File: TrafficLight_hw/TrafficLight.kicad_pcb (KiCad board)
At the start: 2 copper layers, 50 x 104.5 mm, 80 parts, among them Q1 BC848, Q2 MMBT2222, Q3 MMBT2222, SW1 SWITCH, SW2 DIPx6

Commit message: Proceeding with PCB
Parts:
- moved R6 76.6 mm to (139.2, 133.8), turned to 180 degrees
- moved L1 69.2 mm to (133.0, 85.0), turned to 270 degrees
- moved R14 65.5 mm to (147.6, 128.4)
- moved R13 63.2 mm to (134.8, 122.8), turned to 90 degrees
- moved R7 61.2 mm to (135.8, 133.8), turned to 180 degrees
- moved C25 59.4 mm to (142.8, 131.8), turned to 90 degrees
- moved DA1 55.3 mm to (153.2, 131.0), turned to 90 degrees
- moved R12 53.6 mm to (134.8, 119.2), turned to 90 degrees
- moved R2 51.4 mm to (149.0, 100.2), turned to 270 degrees
- moved Q2 48.2 mm to (137.8, 122.8), turned to 90 degrees
- moved Q1 46.3 mm to (137.8, 119.2), turned to 90 degrees
- moved R5 45.9 mm to (139.0, 110.2), turned to 270 degrees
- moved C24 43.5 mm to (144.6, 131.4), turned to 90 degrees
- moved C14 43.4 mm to (155.6, 131.0), turned to 270 degrees
- moved Q3 40.1 mm to (147.6, 131.4)
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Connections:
- L1 pad 2: +BATT -> +3.3V
- L2 pad 2: +BATT -> +3.3V
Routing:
- net GND: track 0.00 -> 264.3 mm, vias 0 -> 10
- net VCC: track 0.00 -> 56.9 mm, vias 0 -> 6
- net PwrMCU: track 0.00 -> 50.2 mm, vias 0 -> 4
- net +BATT: track 0.00 -> 39.5 mm
- net /IR_LED: track 0.00 -> 33.3 mm
- net /CC_MOSI: track 0.00 -> 29.1 mm, vias 0 -> 2
- net /CC_GDO2: track 0.00 -> 27.6 mm, vias 0 -> 2
- net /CC_MISO: track 0.00 -> 27.5 mm, vias 0 -> 2
- net /CC_SCK: track 0.00 -> 26.8 mm, vias 0 -> 2
- net /CC_CS: track 0.00 -> 24.5 mm
- net /CC_GDO0: track 0.00 -> 22.1 mm
- net Net-(C15-Pad1): track 0.00 -> 10.5 mm
- net Net-(C19-Pad1): track 0.00 -> 8.78 mm
- net /BAT_IN: track 0.00 -> 8.75 mm
- net /IR_LED_OUT: track 0.00 -> 7.63 mm
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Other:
- net class Default: trace_width 0.25 -> 0.2; via_dia 0.6 -> 0.7; via_drill 0.4 -> 0.3
- net class Wide added: clearance 0.2, trace_width 0.5, via_dia 0.9, via_drill 0.4

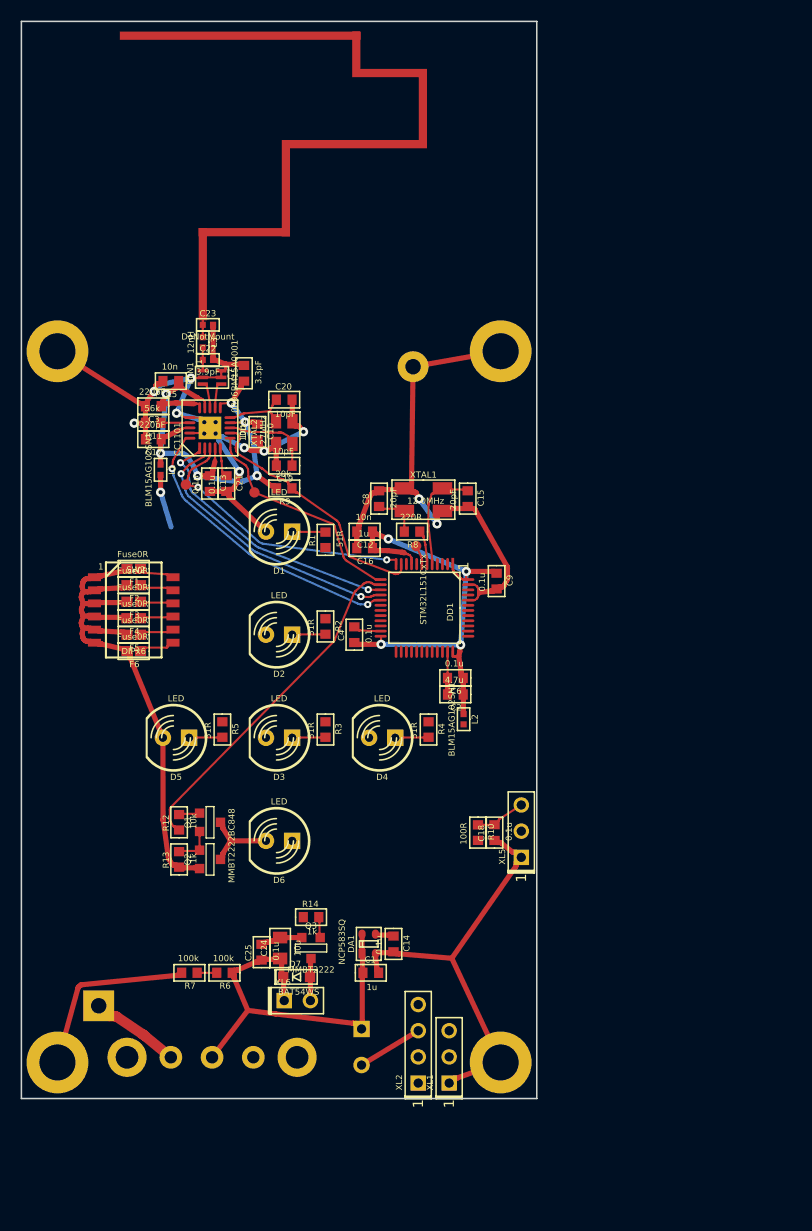
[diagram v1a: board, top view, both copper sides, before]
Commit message: + PCB routing completed
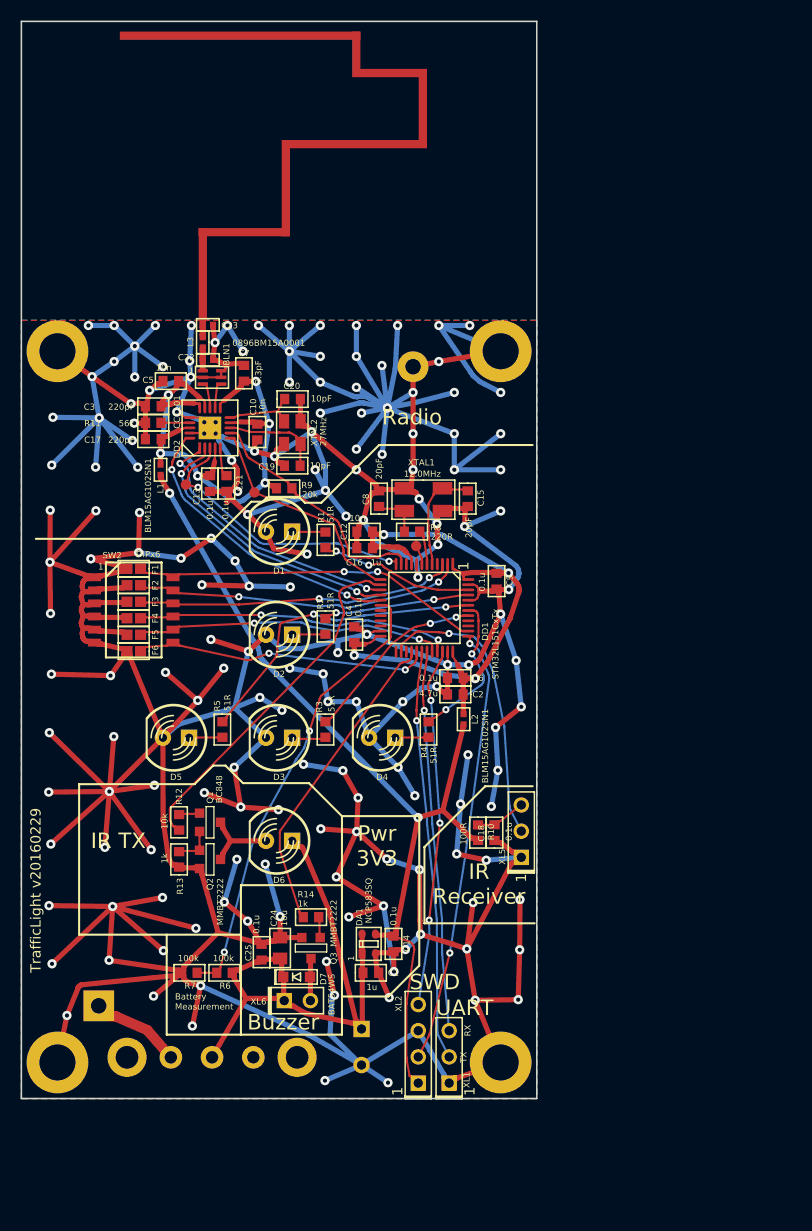
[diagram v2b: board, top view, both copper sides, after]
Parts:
- moved C20 0.80 mm to (145.8, 78.1)
- moved C19 0.78 mm to (145.8, 84.6)
- moved XTAL2 0.78 mm to (145.8, 81.4)
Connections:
- XL2 pad 1: PwrMCU -> +3.3V
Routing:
- net GND: track 264.3 -> 975.2 mm, vias 10 -> 168
- net +3.3V: track 7.05 -> 87.5 mm, vias 1 -> 2
- net /SWCLK: track 0.00 -> 42.4 mm, vias 0 -> 2
- net /BAT_MEAS: track 1.90 -> 43.6 mm, vias 0 -> 2
- net /UART_TX: track 0.00 -> 39.7 mm, vias 0 -> 1
- net /UART_RX: track 0.00 -> 36.9 mm, vias 0 -> 1
- net /SWDIO: track 0.00 -> 34.8 mm, vias 0 -> 3
- net /Buzzer: track 0.00 -> 30.7 mm
- net /DS1: track 3.38 -> 34.0 mm, vias 0 -> 2
- net /LEFT_LED: track 0.00 -> 30.0 mm, vias 0 -> 2
- net /DS2: track 3.27 -> 31.7 mm, vias 0 -> 2
- net /IR_RX: track 0.00 -> 28.0 mm, vias 0 -> 1
- net /DS3: track 3.16 -> 30.7 mm, vias 0 -> 2
- net /DS4: track 3.16 -> 30.5 mm, vias 0 -> 2
- net /DS5: track 3.27 -> 29.6 mm, vias 0 -> 2
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- added copper zone on B.Cu, net GND
- added copper zone on F.Cu, net GND
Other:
- rule pad_to_mask_clearance: 0.2 -> 0.1
- board text added: "Battery Measurement"
- board text added: "Buzzer"
- board text added: "IR Receiver"
- board text added: "IR TX"
- board text added: "Pwr 3V3"
- board text added: "RX"
- board text added: "Radio"
- board text added: "SWD"
- board text added: "TX"
- board text added: "TrafficLight v20160229"
- board text added: "UART"

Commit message: + Quantduino PCB
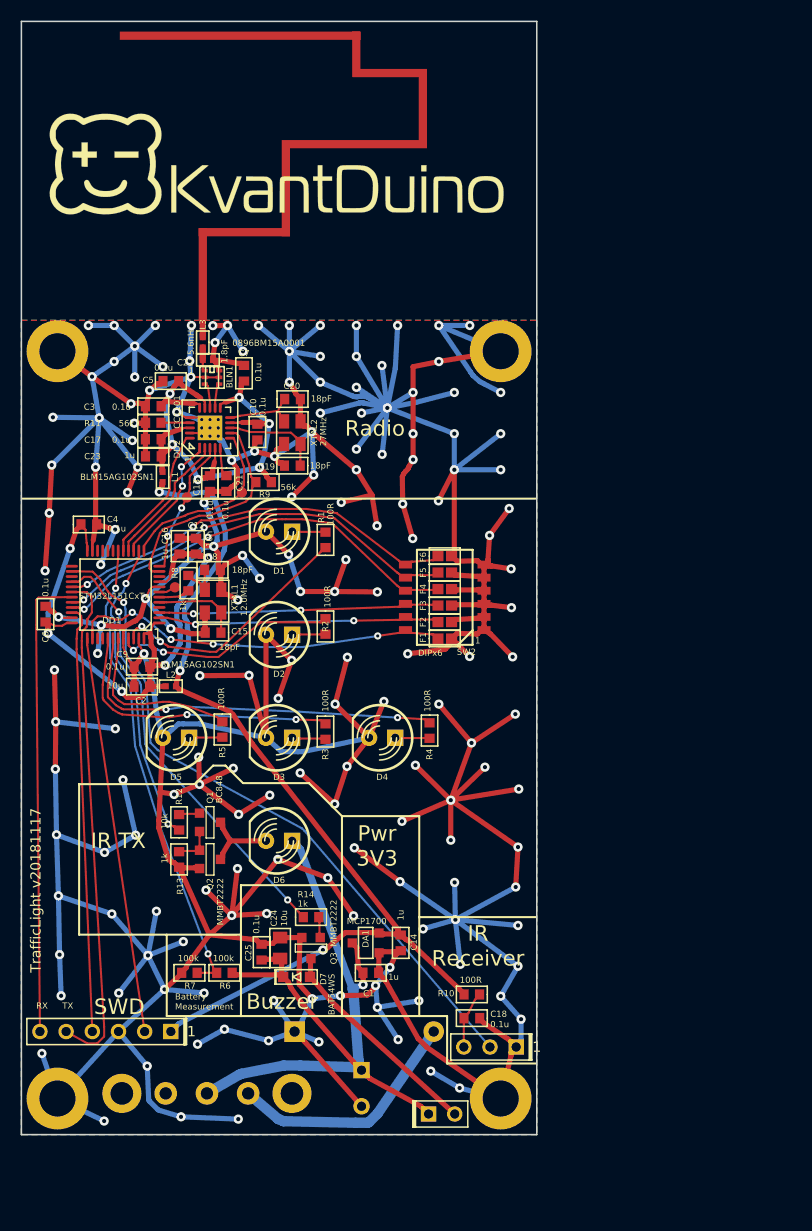
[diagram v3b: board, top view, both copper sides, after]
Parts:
- removed XL2: ST_SWD, Connectors:PLS-4
- removed XL3: CONN_1, Connectors:Square_1MM5
- removed XL4: CONN_1, Connectors:Round_1MM5
- added B1: BAT, Installation:BAT_HOLDER_3xAA, B.Cu at (144.5, 106.0)
- added Logo1: Logo, Pictures:KvantduinoLogoText_44d4, F.Cu at (144.2, 55.3)
- added Logo3: Logo, Pictures:MadeInRussia_47d4, B.Cu at (144.5, 67.0)
- ANT1: footprint Radio:ANT_868_MEANDER_4HOR_35mm -> Antennas:ANT_868_MEANDER_4HOR_35mm
- C10, C5: value 10n -> 0.1u
- C14: value 0.1u -> 1u
- C15, C8: value 20pF -> 18pF
- C17, C3: value 220pF -> 0.1u
- C19, C20: value 10pF -> 18pF
- C2: value 4.7u -> 10u
- C22: value 3.9pF -> 1.8pF
- C23: value DoNotMount -> 1u; footprint Capacitors:CAP_0402 -> Capacitors:CAP_0603
- C7: value 3.3pF -> 0.1u
- DA1: value NCP583SQ -> MCP1700; footprint SOT:SC82AB -> SOT:SOT23-3A
- L3: value 12nH -> 5.6nH
- R1, R2, R3, R4, R5: value 51R -> 100R
- R8: value 220R -> 1k
- R9: value 20k -> 56k
- XL1: value CONN_3 -> CONN_6; footprint Connectors:PLS-3 -> Connectors:PLS-6; moved to B.Cu
- XL5, XL6: moved to B.Cu
- XTAL1: footprint Quartz:0503x4-4 -> Quartz:03225C4
- moved C6 40.2 mm to (121.8, 99.0), turned to 90 degrees
- moved C9 35.4 mm to (131.2, 104.1), turned to 180 degrees
- moved F6 31.6 mm to (160.6, 93.4), turned to 0 degrees
- moved F1 30.9 mm to (160.6, 101.4), turned to 0 degrees
- moved F5 30.8 mm to (160.6, 95.0), turned to 0 degrees
- moved C2 30.4 mm to (131.2, 106.0)
- moved F2 30.4 mm to (160.6, 99.8), turned to 0 degrees
- moved F4 30.3 mm to (160.6, 96.6), turned to 0 degrees
- moved SW2 30.2 mm to (160.6, 97.4), turned to 180 degrees
- moved F3 30.2 mm to (160.6, 98.2), turned to 0 degrees
- moved DD1 30.0 mm to (128.6, 97.1), turned to 180 degrees
- moved L2 28.6 mm to (134.0, 106.0), turned to 0 degrees
- moved C15 27.9 mm to (138.1, 100.8), turned to 180 degrees
- moved C4 27.9 mm to (126.0, 90.3), turned to 0 degrees
- moved XL1 27.5 mm to (134.0, 139.5), turned to 180 degrees
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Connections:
- C23 pad 1: /ANT2 -> VCC
- DA1 pad 1: +BATT -> GND
- DA1 pad 2: GND -> +3.3V
- DA1 pad 3: +3.3V -> +BATT
- XL1 pad 1: GND -> +3.3V
- XL1 pad 2: /UART_TX -> /SWCLK
- XL1 pad 3: /UART_RX -> GND
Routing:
- net /IR_RX: track 28.0 -> 65.5 mm
- net /RIGHT_LED: track 14.8 -> 37.6 mm
- net /VibroOut: track 4.10 -> 21.2 mm
- net /CC_MOSI: track 28.9 -> 13.4 mm, vias 2 -> 0
- net +BATT: track 59.8 -> 74.5 mm, vias 0 -> 1
- net /BAT_IN: track 8.90 -> 23.5 mm
- net /CC_GDO2: track 27.7 -> 13.3 mm
- net /CC_MISO: track 27.4 -> 13.0 mm, vias 2 -> 0
- net /CC_SCK: track 26.9 -> 12.6 mm
- net /LEFT_LED: track 30.0 -> 16.9 mm, vias 2 -> 0
- net /Buzzer: track 30.7 -> 42.6 mm, vias 0 -> 2
- net /ANT2: track 6.11 -> 17.2 mm
- net /DS6: track 28.6 -> 39.3 mm
- net /DS5: track 29.6 -> 40.1 mm
- net /STRAIGHT_LED: track 18.1 -> 28.2 mm
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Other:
- board size 50 x 104.5 mm -> 50 x 108 mm
- board text added: "TrafficLight v20181117"
- board text removed: "TrafficLight v20160229"
- board text removed: "UART"
